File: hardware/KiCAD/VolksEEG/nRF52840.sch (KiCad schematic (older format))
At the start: 5 parts, among them J2 693061010911, U2 nRF52840-Feather-Sense

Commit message: Some re-naming and added some pull ups to the nrf schematic.
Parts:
- added R? (x2): R, Resistor_SMD:R_0603_1608Metric_Pad0.98x0.95mm_HandSolder, symbol Device:R
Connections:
- net labels added: +3V3_nrf, ADS-DRDY_nrf, ADS-nCS_nrf, ADS-nRST_nrf, MISO_nrf, MOSI_nrf, SCK_nrf, SD-nCD_nrf, SD-nCS_nrf
- net labels removed: ADS-nRST, MISO, MOSI, SCK, SD_nCD, nCS0, nCS1
- wire segments 38 -> 52
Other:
- moved on the sheet: R17
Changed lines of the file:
@@
 $Descr A4 11693 8268
 encoding utf-8
-Sheet 5 6
+Sheet 4 6
 Title ""
 Date ""
@@
 $EndDescr
 Text HLabel 6800 3400 2    50   Output ~ 0
-MOSI
+MOSI_nrf
 Text HLabel 6800 3500 2    50   Output ~ 0
-SCK
+SCK_nrf
 Text HLabel 6800 3300 2    50   Input ~ 0
-MISO
-Text HLabel 4100 3700 0    50   Output ~ 0
-nCS0
-Text HLabel 4100 3900 0    50   Output ~ 0
-ADS-nRST
-Wire Wire Line
-	5050 3700 4500 3700
-Wire Wire Line
-	5050 3900 4100 3900
+MISO_nrf
+Text HLabel 3400 3900 0    50   Output ~ 0
+ADS-nCS_nrf
+Text HLabel 3400 4000 0    50   Output ~ 0
+ADS-nRST_nrf
 Wire Wire Line
 	6050 3300 6800 3300
@@
 	1    0    0    -1
 $EndComp
-Text HLabel 4100 3800 0    50   Output ~ 0
-nCS1
-Wire Wire Line
-	5050 3800 4750 3800
 $Comp
 L Device:R R17
 U 1 1 61650065
-P 4500 3350
-F 0 "R17" H 4570 3396 50  0000 L CNN
-F 1 "R" H 4570 3305 50  0000 L CNN
-F 2 "Resistor_SMD:R_0603_1608Metric_Pad0.98x0.95mm_HandSolder" V 4430 3350 50  0001 C CNN
-F 3 "~" H 4500 3350 50  0001 C CNN
-	1    4500 3350
+P 4450 3350
+F 0 "R17" H 4520 3396 50  0000 L CNN
+F 1 "R" H 4520 3305 50  0000 L CNN
+F 2 "Resistor_SMD:R_0603_1608Metric_Pad0.98x0.95mm_HandSolder" V 4380 3350 50  0001 C CNN
+F 3 "~" H 4450 3350 50  0001 C CNN
+	1    4450 3350
 	1    0    0    -1
 $EndComp
@@
 	1    0    0    -1
 $EndComp
-$Comp
-L power:VDC #PWR0101
-U 1 1 61650AD7
-P 4500 3100
-F 0 "#PWR0101" H 4500 3000 50  0001 C CNN
-F 1 "VDC" H 4515 3273 50  0000 C CNN
-F 2 "" H 4500 3100 50  0001 C CNN
-F 3 "" H 4500 3100 50  0001 C CNN
-	1    4500 3100
-	1    0    0    -1
-$EndComp
-$Comp
-L power:VDC #PWR0102
-U 1 1 61650CE3
-P 4750 3100
-F 0 "#PWR0102" H 4750 3000 50  0001 C CNN
-F 1 "VDC" H 4765 3273 50  0000 C CNN
-F 2 "" H 4750 3100 50  0001 C CNN
-F 3 "" H 4750 3100 50  0001 C CNN
-	1    4750 3100
-	1    0    0    -1
-$EndComp
-Connection ~ 4500 3700
-Wire Wire Line
-	4500 3700 4100 3700
-Wire Wire Line
-	4750 3500 4750 3800
-Connection ~ 4750 3800
-Wire Wire Line
-	4750 3800 4100 3800
-Wire Wire Line
-	4500 3500 4500 3700
-Wire Wire Line
-	4750 3200 4750 3100
-Wire Wire Line
-	4500 3100 4500 3200
 Text Label 8650 1850 0    50   ~ 0
-nCS1
+SD-nCS_nrf
 Text Label 8650 1950 0    50   ~ 0
-MOSI
+MOSI_nrf
 Text Label 8650 2450 0    50   ~ 0
-MISO
+MISO_nrf
 Text Label 8650 2250 0    50   ~ 0
-SCK
+SCK_nrf
 Text Label 8650 2750 0    50   ~ 0
-SD_nCD
+SD-nCD_nrf
 $Comp
 L power:VDC #PWR0103
@@
 Text Label 8100 4650 0    50   ~ 0
 SCL
+Text HLabel 3400 4100 0    50   Input ~ 0
+ADS-DRDY_nrf
+Text Label 3400 3700 2    50   ~ 0
+SD-nCD_nrf
+Text HLabel 6800 2700 2    50   Output ~ 0
++3V3_nrf
+Connection ~ 6200 2700
+Wire Wire Line
+	6200 2700 6800 2700
+$Comp
+L Device:R R?
+U 1 1 61746C2B
+P 4150 3350
+F 0 "R?" H 4220 3396 50  0000 L CNN
+F 1 "R" H 4220 3305 50  0000 L CNN
+F 2 "Resistor_SMD:R_0603_1608Metric_Pad0.98x0.95mm_HandSolder" V 4080 3350 50  0001 C CNN
+F 3 "~" H 4150 3350 50  0001 C CNN
+	1    4150 3350
+	1    0    0    -1
+$EndComp
+Text Label 3400 3800 2    50   ~ 0
+SD-nCS_nrf
+$Comp
+L Device:R R?
+U 1 1 6174C834
+P 3850 3350
+F 0 "R?" H 3920 3396 50  0000 L CNN
+F 1 "R" H 3920 3305 50  0000 L CNN
+F 2 "Resistor_SMD:R_0603_1608Metric_Pad0.98x0.95mm_HandSolder" V 3780 3350 50  0001 C CNN
+F 3 "~" H 3850 3350 50  0001 C CNN
+	1    3850 3350
+	1    0    0    -1
+$EndComp
+Wire Wire Line
+	3400 3900 4450 3900
+Wire Wire Line
+	3400 3700 3850 3700
+Wire Wire Line
+	3400 3800 4150 3800
+$Comp
+L power:VDC #PWR?
+U 1 1 6174E817
+P 4300 2950
+F 0 "#PWR?" H 4300 2850 50  0001 C CNN
+F 1 "VDC" H 4315 3123 50  0000 C CNN
+F 2 "" H 4300 2950 50  0001 C CNN
+F 3 "" H 4300 2950 50  0001 C CNN
+	1    4300 2950
+	1    0    0    -1
+$EndComp
+Wire Wire Line
+	3400 4000 4750 4000
+Wire Wire Line
+	3850 3500 3850 3700
+Connection ~ 3850 3700
+Wire Wire Line
+	3850 3700 5050 3700
+Wire Wire Line
+	4150 3500 4150 3800
+Connection ~ 4150 3800
+Wire Wire Line
+	4150 3800 5050 3800
+Wire Wire Line
+	4450 3500 4450 3900
+Connection ~ 4450 3900
+Wire Wire Line
+	4450 3900 5050 3900
+Wire Wire Line
+	4750 3500 4750 4000
+Connection ~ 4750 4000
+Wire Wire Line
+	4750 4000 5050 4000
+Wire Wire Line
+	4300 3100 4150 3100
+Wire Wire Line
+	3850 3100 3850 3200
+Wire Wire Line
+	4150 3200 4150 3100
+Connection ~ 4150 3100
+Wire Wire Line
+	4150 3100 3850 3100
+Wire Wire Line
+	4750 3200 4750 3100
+Wire Wire Line
+	4750 3100 4450 3100
+Connection ~ 4300 3100
+Wire Wire Line
+	4450 3200 4450 3100
+Connection ~ 4450 3100
+Wire Wire Line
+	4450 3100 4300 3100
+Wire Wire Line
+	4300 2950 4300 3100
+Wire Wire Line
+	3400 4100 5050 4100
 $EndSCHEMATC

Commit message: Added Digi-key's kicad component libraries, some work done on power, think this will change but capturing it here for posterity.
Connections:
- net labels added: ADS-nDRDY_nrf
- net labels removed: ADS-DRDY_nrf
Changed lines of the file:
@@
 SCL
 Text HLabel 3400 4100 0    50   Input ~ 0
-ADS-DRDY_nrf
+ADS-nDRDY_nrf
 Text Label 3400 3700 2    50   ~ 0
 SD-nCD_nrf

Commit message: Added more tasks following re-watch of 1st half of previous design review.
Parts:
- U2: value nRF52840-Feather-Sense -> nRF52840-Feather-Sense-Board
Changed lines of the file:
@@
 P 5550 3550
 F 0 "U2" H 5550 4665 50  0000 C CNN
-F 1 "nRF52840-Feather-Sense" H 5550 4574 50  0000 C CNN
+F 1 "nRF52840-Feather-Sense-Board" H 5450 4600 50  0000 C CNN
 F 2 "VolksEEG:nRF52840_Feather_Sense" H 5200 4550 50  0001 C CNN
 F 3 "https://cdn-learn.adafruit.com/downloads/pdf/adafruit-feather-sense.pdf" H 5200 4550 50  0001 C CNN

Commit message: Updated names of heirarchical pins, finished referential montage configuration, added filter cap to ADS_nRST line, started putting ADS1299 gpios to a header.
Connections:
- net labels added: +3V3_ni, ADS-nCS_ni, ADS-nDRDY_ni, ADS-nRST_ni, MISO_ni, MOSI_ni, SCK_ni, SCL_ni, SD-nCD_ni, SD-nCS_ni, SDA_ni
- net labels removed: +3V3_nrf, ADS-nCS_nrf, ADS-nDRDY_nrf, ADS-nRST_nrf, MISO_nrf, MOSI_nrf, SCK_nrf, SCL, SD-nCD_nrf, SD-nCS_nrf, SDA
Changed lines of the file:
@@
 $EndDescr
 Text HLabel 6800 3400 2    50   Output ~ 0
-MOSI_nrf
+MOSI_ni
 Text HLabel 6800 3500 2    50   Output ~ 0
-SCK_nrf
+SCK_ni
 Text HLabel 6800 3300 2    50   Input ~ 0
-MISO_nrf
+MISO_ni
 Text HLabel 3400 3900 0    50   Output ~ 0
-ADS-nCS_nrf
+ADS-nCS_ni
 Text HLabel 3400 4000 0    50   Output ~ 0
-ADS-nRST_nrf
+ADS-nRST_ni
 Wire Wire Line
 	6050 3300 6800 3300
@@
 $EndComp
 Text Label 8650 1850 0    50   ~ 0
-SD-nCS_nrf
+SD-nCS_ni
 Text Label 8650 1950 0    50   ~ 0
-MOSI_nrf
+MOSI_ni
 Text Label 8650 2450 0    50   ~ 0
-MISO_nrf
+MISO_ni
 Text Label 8650 2250 0    50   ~ 0
-SCK_nrf
+SCK_ni
 Text Label 8650 2750 0    50   ~ 0
-SD-nCD_nrf
+SD-nCD_ni
 $Comp
 L power:VDC #PWR0103
 U 1 1 61652DA7
-P 8950 1700
-F 0 "#PWR0103" H 8950 1600 50  0001 C CNN
-F 1 "VDC" H 8965 1873 50  0000 C CNN
-F 2 "" H 8950 1700 50  0001 C CNN
-F 3 "" H 8950 1700 50  0001 C CNN
-	1    8950 1700
-	1    0    0    -1
-$EndComp
-Wire Wire Line
-	9100 2050 9000 2050
-Wire Wire Line
-	9000 2050 9000 2350
-Wire Wire Line
-	9100 2350 9000 2350
-Connection ~ 9000 2350
-Wire Wire Line
-	9000 2350 9000 3250
-Wire Wire Line
-	9100 2150 8950 2150
-Wire Wire Line
-	8950 2150 8950 1700
-Wire Wire Line
-	9600 3250 9000 3250
-Wire Wire Line
-	9000 3350 9000 3250
-Connection ~ 9000 3250
+P 8400 1700
+F 0 "#PWR0103" H 8400 1600 50  0001 C CNN
+F 1 "VDC" H 8415 1873 50  0000 C CNN
+F 2 "" H 8400 1700 50  0001 C CNN
+F 3 "" H 8400 1700 50  0001 C CNN
+	1    8400 1700
+	1    0    0    -1
+$EndComp
+Wire Wire Line
+	9100 2050 8550 2050
+Wire Wire Line
+	8550 2050 8550 2350
+Wire Wire Line
+	9100 2350 8550 2350
+Connection ~ 8550 2350
+Wire Wire Line
+	8550 2350 8550 3250
+Wire Wire Line
+	9100 2150 8400 2150
+Wire Wire Line
+	8400 2150 8400 1700
+Wire Wire Line
+	9600 3250 8550 3250
+Wire Wire Line
+	8550 3350 8550 3250
+Connection ~ 8550 3250
 Wire Wire Line
 	9100 2250 8650 2250
@@
 L power:GNDD #PWR?
 U 1 1 6181E9E7
-P 9000 3350
-F 0 "#PWR?" H 9000 3100 50  0001 C CNN
-F 1 "GNDD" H 9004 3195 50  0000 C CNN
-F 2 "" H 9000 3350 50  0001 C CNN
-F 3 "" H 9000 3350 50  0001 C CNN
-	1    9000 3350
+P 8550 3350
+F 0 "#PWR?" H 8550 3100 50  0001 C CNN
+F 1 "GNDD" H 8554 3195 50  0000 C CNN
+F 2 "" H 8550 3350 50  0001 C CNN
+F 3 "" H 8550 3350 50  0001 C CNN
+	1    8550 3350
 	1    0    0    -1
 $EndComp
 Text Label 8100 4550 0    50   ~ 0
-SDA
+SDA_ni
 Text Label 8100 4650 0    50   ~ 0
-SCL
+SCL_ni
 Text HLabel 3400 4100 0    50   Input ~ 0
-ADS-nDRDY_nrf
+ADS-nDRDY_ni
 Text Label 3400 3700 2    50   ~ 0
-SD-nCD_nrf
+SD-nCD_ni
 Text HLabel 6800 2700 2    50   Output ~ 0
-+3V3_nrf
++3V3_ni
 Connection ~ 6200 2700
 Wire Wire Line
@@
 $EndComp
 Text Label 3400 3800 2    50   ~ 0
-SD-nCS_nrf
+SD-nCS_ni
 $Comp
 L Device:R R?

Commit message: Added custom power symbols for non isolated power. Seperated Analogue and digital supplies. finished putting the ADS1299 GPIOs to a header.
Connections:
- net labels added: GND_ni
- net labels removed: GNDD, VDC
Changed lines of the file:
@@
 	6200 2700 6200 2550
-$Comp
-L power:VDC #PWR06
-U 1 1 61617FBE
-P 6200 2550
-F 0 "#PWR06" H 6200 2450 50  0001 C CNN
-F 1 "VDC" H 6215 2723 50  0000 C CNN
-F 2 "" H 6200 2550 50  0001 C CNN
-F 3 "" H 6200 2550 50  0001 C CNN
-	1    6200 2550
-	1    0    0    -1
-$EndComp
 $Comp
 L VolksEEG:nRF52840-Feather-Sense U2
@@
 Text Label 8650 2750 0    50   ~ 0
 SD-nCD_ni
-$Comp
-L power:VDC #PWR0103
-U 1 1 61652DA7
-P 8400 1700
-F 0 "#PWR0103" H 8400 1600 50  0001 C CNN
-F 1 "VDC" H 8415 1873 50  0000 C CNN
-F 2 "" H 8400 1700 50  0001 C CNN
-F 3 "" H 8400 1700 50  0001 C CNN
-	1    8400 1700
-	1    0    0    -1
-$EndComp
 Wire Wire Line
 	9100 2050 8550 2050
@@
 Wire Wire Line
 	9100 4350 9100 4850
-$Comp
-L power:VDC #PWR?
-U 1 1 61661CFB
-P 9000 4200
-F 0 "#PWR?" H 9000 4100 50  0001 C CNN
-F 1 "VDC" H 9015 4373 50  0000 C CNN
-F 2 "" H 9000 4200 50  0001 C CNN
-F 3 "" H 9000 4200 50  0001 C CNN
-	1    9000 4200
-	1    0    0    -1
-$EndComp
 Text Notes 6200 3850 0    50   ~ 0
 Pull-ups are on the nRF preinstalled
-$Comp
-L power:GNDD #PWR?
-U 1 1 6181C322
-P 6050 4550
-F 0 "#PWR?" H 6050 4300 50  0001 C CNN
-F 1 "GNDD" H 6054 4395 50  0000 C CNN
-F 2 "" H 6050 4550 50  0001 C CNN
-F 3 "" H 6050 4550 50  0001 C CNN
-	1    6050 4550
-	1    0    0    -1
-$EndComp
-$Comp
-L power:GNDD #PWR?
-U 1 1 6181E17F
-P 9100 4850
-F 0 "#PWR?" H 9100 4600 50  0001 C CNN
-F 1 "GNDD" H 9104 4695 50  0000 C CNN
-F 2 "" H 9100 4850 50  0001 C CNN
-F 3 "" H 9100 4850 50  0001 C CNN
-	1    9100 4850
-	1    0    0    -1
-$EndComp
-$Comp
-L power:GNDD #PWR?
-U 1 1 6181E9E7
-P 8550 3350
-F 0 "#PWR?" H 8550 3100 50  0001 C CNN
-F 1 "GNDD" H 8554 3195 50  0000 C CNN
-F 2 "" H 8550 3350 50  0001 C CNN
-F 3 "" H 8550 3350 50  0001 C CNN
-	1    8550 3350
-	1    0    0    -1
-$EndComp
 Text Label 8100 4550 0    50   ~ 0
 SDA_ni
@@
 Wire Wire Line
 	3400 3800 4150 3800
-$Comp
-L power:VDC #PWR?
-U 1 1 6174E817
+Wire Wire Line
+	3400 4000 4750 4000
+Wire Wire Line
+	3850 3500 3850 3700
+Connection ~ 3850 3700
+Wire Wire Line
+	3850 3700 5050 3700
+Wire Wire Line
+	4150 3500 4150 3800
+Connection ~ 4150 3800
+Wire Wire Line
+	4150 3800 5050 3800
+Wire Wire Line
+	4450 3500 4450 3900
+Connection ~ 4450 3900
+Wire Wire Line
+	4450 3900 5050 3900
+Wire Wire Line
+	4750 3500 4750 4000
+Connection ~ 4750 4000
+Wire Wire Line
+	4750 4000 5050 4000
+Wire Wire Line
+	4300 3100 4150 3100
+Wire Wire Line
+	3850 3100 3850 3200
+Wire Wire Line
+	4150 3200 4150 3100
+Connection ~ 4150 3100
+Wire Wire Line
+	4150 3100 3850 3100
+Wire Wire Line
+	4750 3200 4750 3100
+Wire Wire Line
+	4750 3100 4450 3100
+Connection ~ 4300 3100
+Wire Wire Line
+	4450 3200 4450 3100
+Connection ~ 4450 3100
+Wire Wire Line
+	4450 3100 4300 3100
+Wire Wire Line
+	4300 2950 4300 3100
+Wire Wire Line
+	3400 4100 5050 4100
+$Comp
+L VolksEEG:+3V3_ni #PWR?
+U 1 1 61BCCA44
+P 8400 1700
+F 0 "#PWR?" H 8400 1550 50  0001 C CNN
+F 1 "+3V3_ni" H 8415 1873 50  0000 C CNN
+F 2 "" H 8400 1700 50  0001 C CNN
+F 3 "" H 8400 1700 50  0001 C CNN
+	1    8400 1700
+	1    0    0    -1
+$EndComp
+$Comp
+L VolksEEG:+3V3_ni #PWR?
+U 1 1 61BCCD8D
+P 9000 4200
+F 0 "#PWR?" H 9000 4050 50  0001 C CNN
+F 1 "+3V3_ni" H 9015 4373 50  0000 C CNN
+F 2 "" H 9000 4200 50  0001 C CNN
+F 3 "" H 9000 4200 50  0001 C CNN
+	1    9000 4200
+	1    0    0    -1
+$EndComp
+$Comp
+L VolksEEG:+3V3_ni #PWR?
+U 1 1 61BCD276
+P 6200 2550
+F 0 "#PWR?" H 6200 2400 50  0001 C CNN
+F 1 "+3V3_ni" H 6215 2723 50  0000 C CNN
+F 2 "" H 6200 2550 50  0001 C CNN
+F 3 "" H 6200 2550 50  0001 C CNN
+	1    6200 2550
+	1    0    0    -1
+$EndComp
+$Comp
+L VolksEEG:+3V3_ni #PWR?
+U 1 1 61BCEE26
 P 4300 2950
-F 0 "#PWR?" H 4300 2850 50  0001 C CNN
-F 1 "VDC" H 4315 3123 50  0000 C CNN
+F 0 "#PWR?" H 4300 2800 50  0001 C CNN
+F 1 "+3V3_ni" H 4315 3123 50  0000 C CNN
 F 2 "" H 4300 2950 50  0001 C CNN
 F 3 "" H 4300 2950 50  0001 C CNN
@@
 	1    0    0    -1
 $EndComp
-Wire Wire Line
-	3400 4000 4750 4000
-Wire Wire Line
-	3850 3500 3850 3700
-Connection ~ 3850 3700
-Wire Wire Line
-	3850 3700 5050 3700
-Wire Wire Line
-	4150 3500 4150 3800
-Connection ~ 4150 3800
-Wire Wire Line
-	4150 3800 5050 3800
-Wire Wire Line
-	4450 3500 4450 3900
-Connection ~ 4450 3900
-Wire Wire Line
-	4450 3900 5050 3900
-Wire Wire Line
-	4750 3500 4750 4000
-Connection ~ 4750 4000
-Wire Wire Line
-	4750 4000 5050 4000
-Wire Wire Line
-	4300 3100 4150 3100
-Wire Wire Line
-	3850 3100 3850 3200
-Wire Wire Line
-	4150 3200 4150 3100
-Connection ~ 4150 3100
-Wire Wire Line
-	4150 3100 3850 3100
-Wire Wire Line
-	4750 3200 4750 3100
-Wire Wire Line
-	4750 3100 4450 3100
-Connection ~ 4300 3100
-Wire Wire Line
-	4450 3200 4450 3100
-Connection ~ 4450 3100
-Wire Wire Line
-	4450 3100 4300 3100
-Wire Wire Line
-	4300 2950 4300 3100
-Wire Wire Line
-	3400 4100 5050 4100
+$Comp
+L VolksEEG:GND_ni #PWR?
+U 1 1 61BCF5D6
+P 6050 4550
+F 0 "#PWR?" H 6050 4300 50  0001 C CNN
+F 1 "GND_ni" H 6055 4377 50  0000 C CNN
+F 2 "" H 6050 4550 50  0001 C CNN
+F 3 "" H 6050 4550 50  0001 C CNN
+	1    6050 4550
+	1    0    0    -1
+$EndComp
+$Comp
+L VolksEEG:GND_ni #PWR?
+U 1 1 61BCF9B4
+P 8550 3350
+F 0 "#PWR?" H 8550 3100 50  0001 C CNN
+F 1 "GND_ni" H 8555 3177 50  0000 C CNN
+F 2 "" H 8550 3350 50  0001 C CNN
+F 3 "" H 8550 3350 50  0001 C CNN
+	1    8550 3350
+	1    0    0    -1
+$EndComp
+$Comp
+L VolksEEG:GND_ni #PWR?
+U 1 1 61BD20F9
+P 9100 4850
+F 0 "#PWR?" H 9100 4600 50  0001 C CNN
+F 1 "GND_ni" H 9105 4677 50  0000 C CNN
+F 2 "" H 9100 4850 50  0001 C CNN
+F 3 "" H 9100 4850 50  0001 C CNN
+	1    9100 4850
+	1    0    0    -1
+$EndComp
 $EndSCHEMATC

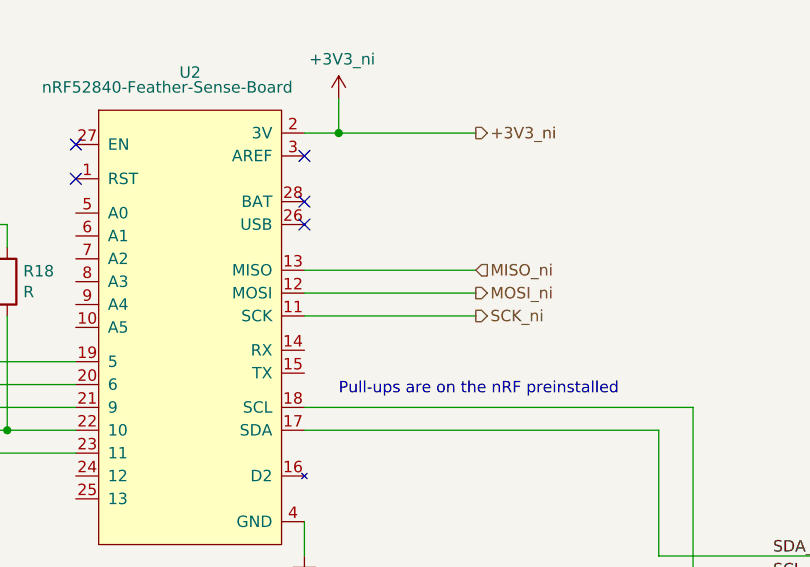
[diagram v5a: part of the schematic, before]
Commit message: Tweaks based on feedback, Changed digital isolators to ADUM240E devices due to component availability.
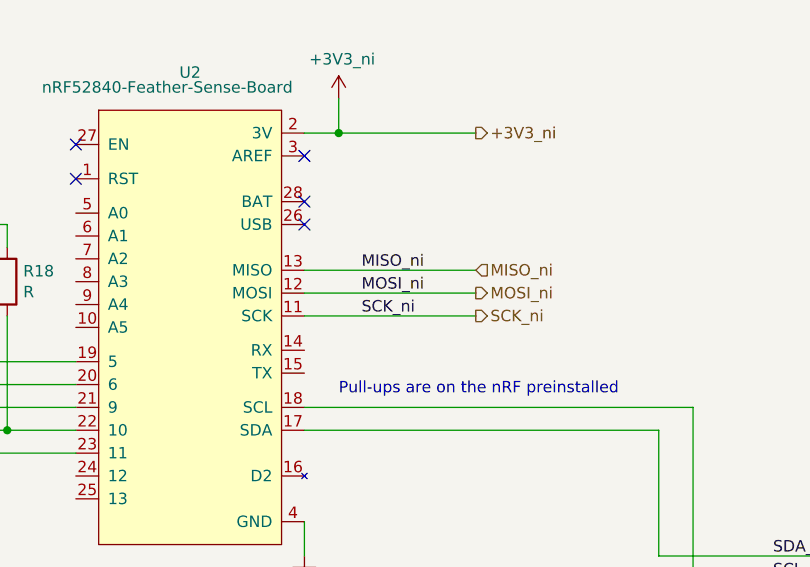
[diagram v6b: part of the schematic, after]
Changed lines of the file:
@@
 	1    0    0    -1
 $EndComp
+Text Label 6300 3300 0    50   ~ 0
+MISO_ni
+Text Label 6300 3400 0    50   ~ 0
+MOSI_ni
+Text Label 6300 3500 0    50   ~ 0
+SCK_ni
 $EndSCHEMATC
